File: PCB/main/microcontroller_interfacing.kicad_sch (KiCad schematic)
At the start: 11 parts, among them IC2 LM358DT, IC3 AT24C256C-SSHL-T, J9 PZ254V-11-02P

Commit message: new PCB
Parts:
- removed MCU1: STM32F030C8Tx, Package_QFP:LQFP-48_7x7mm_P0.5mm, symbol MCU_ST_STM32F0:STM32F030C8Tx
- J9: footprint HDRV2W64P0X254_1X2_508X250X873P -> SamacSys_Parts_Power:HDRV2W64P0X254_1X2_508X250X873P
- TP8, TP9: footprint SamacSys_Parts:5017 -> SamacSys_Parts_Power:5017
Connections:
- net NRST: now reaches C13.1, J9.1
- net SCL_P4 renamed PC15
- net SDA_P43 renamed PB7
- no-connect marks 36 -> 3
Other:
- moved on the sheet: IC3

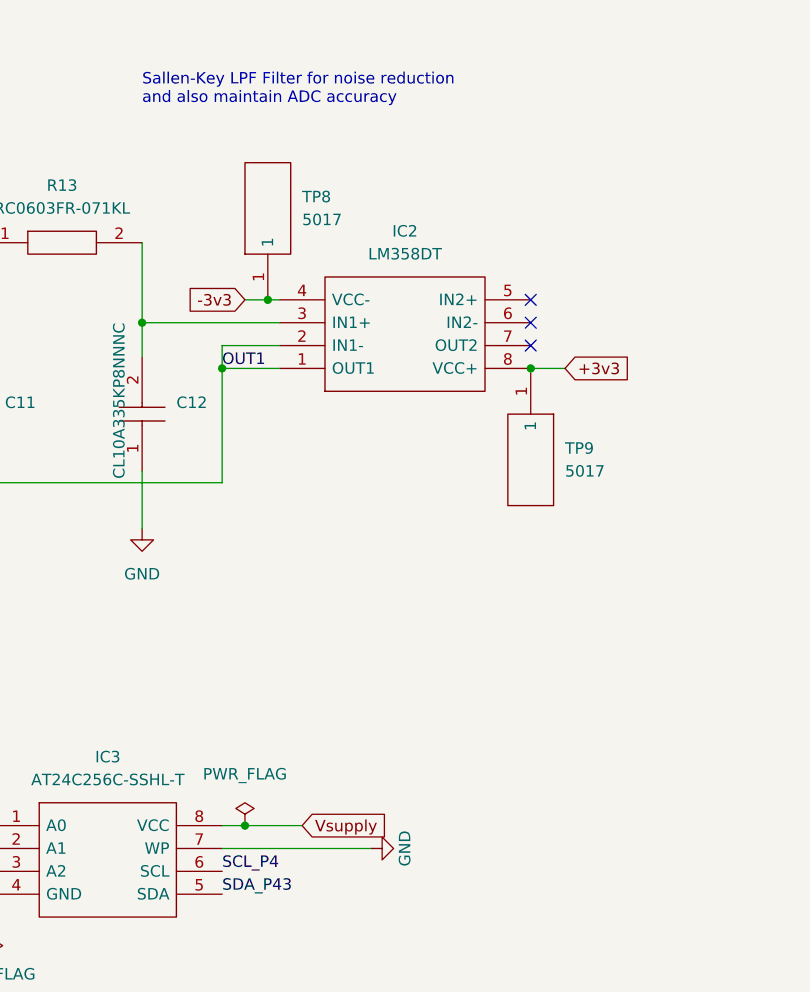
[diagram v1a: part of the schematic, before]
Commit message: changed power schematic
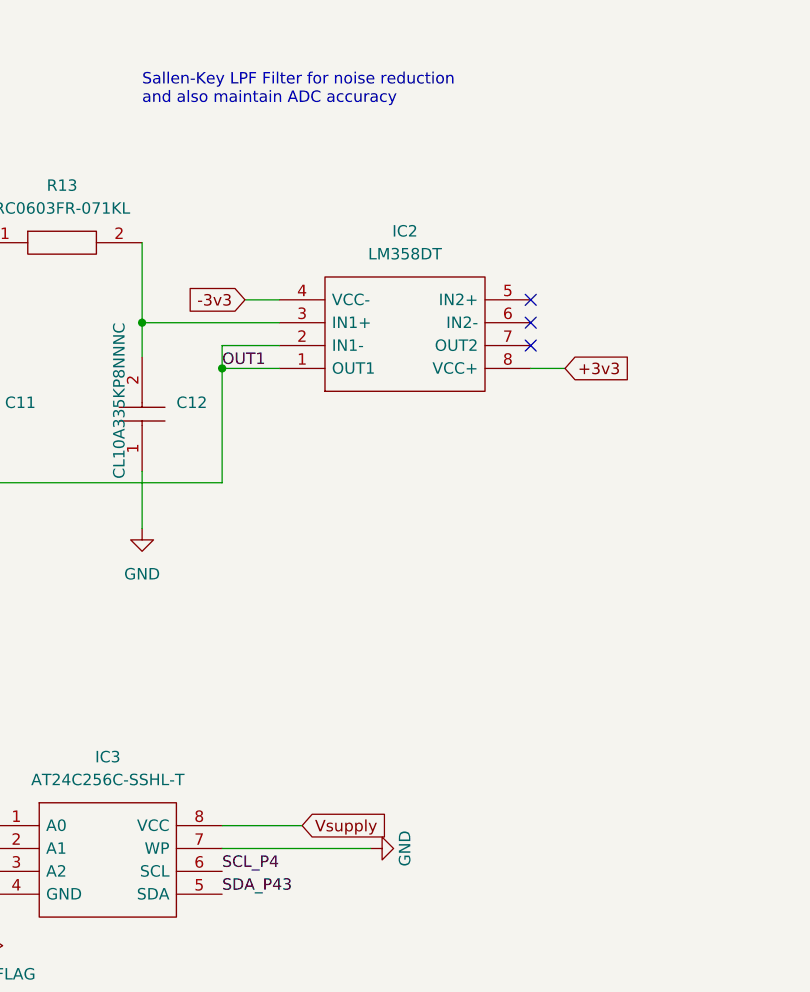
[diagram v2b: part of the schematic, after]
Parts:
- removed TP8, TP9: 5017, SamacSys_Parts_Power:5017, symbol SamacSys_Parts_power:5017
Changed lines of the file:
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@@
   (junction (at 78.74 68.58) (diameter 0) (color 0 0 0 0)
   )
-  (junction (at 121.92 73.66) (diameter 0) (color 0 0 0 0)
-  )
   (junction (at 55.88 127) (diameter 0) (color 0 0 0 0)
   )
-  (junction (at 90.17 124.46) (diameter 0) (color 0 0 0 0)
-  )
   (junction (at 87.63 73.66) (diameter 0) (color 0 0 0 0)
   )
@@
   )
   (junction (at 62.23 132.08) (diameter 0) (color 0 0 0 0)
-  )
-  (junction (at 92.71 66.04) (diameter 0) (color 0 0 0 0)
   )
   (junction (at 180.34 33.02) (diameter 0) (color 0 0 0 0)
@@
     (stroke (width 0) (type default) (color 0 0 0 0))
   )
-  (wire (pts (xy 87.63 124.46) (xy 90.17 124.46))
+  (wire (pts (xy 87.63 124.46) (xy 96.52 124.46))
     (stroke (width 0) (type default) (color 0 0 0 0))
   )
@@
     (stroke (width 0) (type default) (color 0 0 0 0))
   )
-  (wire (pts (xy 90.17 124.46) (xy 96.52 124.46))
-    (stroke (width 0) (type default) (color 0 0 0 0))
-  )
-  (wire (pts (xy 90.17 66.04) (xy 92.71 66.04))
+  (wire (pts (xy 90.17 66.04) (xy 93.98 66.04))
     (stroke (width 0) (type default) (color 0 0 0 0))
   )
@@
   )
   (wire (pts (xy 180.34 33.02) (xy 180.34 38.1))
-    (stroke (width 0) (type default) (color 0 0 0 0))
-  )
-  (wire (pts (xy 92.71 66.04) (xy 93.98 66.04))
     (stroke (width 0) (type default) (color 0 0 0 0))
   )
@@
     )
     (property "Datasheet" "" (id 3) (at 237.49 25.4 0)
-      (effects (font (size 1.27 1.27)) hide)
-    )
-    (pin "1")
-  )
-  (symbol (lib_id "power:PWR_FLAG") (at 90.17 124.46 0) (unit 1)
-    (in_bom yes) (on_board yes) (fields_autoplaced)
-    (property "Reference" "#FLG08" (id 0) (at 90.17 122.555 0)
-      (effects (font (size 1.27 1.27)) hide)
-    )
-    (property "Value" "PWR_FLAG" (id 1) (at 90.17 118.745 0))
-    (property "Footprint" "" (id 2) (at 90.17 124.46 0)
-      (effects (font (size 1.27 1.27)) hide)
-    )
-    (property "Datasheet" "~" (id 3) (at 90.17 124.46 0)
-      (effects (font (size 1.27 1.27)) hide)
-    )
-    (pin "1")
-  )
-  (symbol (lib_id "SamacSys_Parts_power:5017") (at 92.71 66.04 90) (unit 1)
-    (in_bom yes) (on_board yes) (fields_autoplaced)
-    (property "Reference" "TP8" (id 0) (at 96.52 54.6099 90)
-      (effects (font (size 1.27 1.27)) (justify right))
-    )
-    (property "Value" "5017" (id 1) (at 96.52 57.1499 90)
-      (effects (font (size 1.27 1.27)) (justify right))
-    )
-    (property "Footprint" "SamacSys_Parts_Power:5017" (id 2) (at 90.17 49.53 0)
-      (effects (font (size 1.27 1.27)) (justify left) hide)
-    )
-    (property "Datasheet" "http://www.keyelco.com/product.cfm/product_id/1355" (id 3) (at 92.71 49.53 0)
-      (effects (font (size 1.27 1.27)) (justify left) hide)
-    )
-    (property "Description" "KEYSTONE - 5017 - TEST POINT, PCB, MINIATURE, SMT" (id 4) (at 95.25 49.53 0)
-      (effects (font (size 1.27 1.27)) (justify left) hide)
-    )
-    (property "Height" "" (id 5) (at 97.79 49.53 0)
-      (effects (font (size 1.27 1.27)) (justify left) hide)
-    )
-    (property "Manufacturer_Name" "Keystone Electronics" (id 6) (at 100.33 49.53 0)
-      (effects (font (size 1.27 1.27)) (justify left) hide)
-    )
-    (property "Manufacturer_Part_Number" "5017" (id 7) (at 102.87 49.53 0)
-      (effects (font (size 1.27 1.27)) (justify left) hide)
-    )
-    (property "Mouser Part Number" "534-5017" (id 8) (at 105.41 49.53 0)
-      (effects (font (size 1.27 1.27)) (justify left) hide)
-    )
-    (property "Mouser Price/Stock" "https://www.mouser.co.uk/ProductDetail/Keystone-Electronics/5017?qs=Rc9fedAPY0Oq34lsnTvuLg%3D%3D" (id 9) (at 107.95 49.53 0)
-      (effects (font (size 1.27 1.27)) (justify left) hide)
-    )
-    (property "Arrow Part Number" "" (id 10) (at 110.49 49.53 0)
-      (effects (font (size 1.27 1.27)) (justify left) hide)
-    )
-    (property "Arrow Price/Stock" "" (id 11) (at 113.03 49.53 0)
-      (effects (font (size 1.27 1.27)) (justify left) hide)
-    )
-    (property "Comment" "test point" (id 12) (at 92.71 66.04 0)
-      (effects (font (size 1.27 1.27)) hide)
-    )
-    (property "JLCPCB Part Number" "C238130" (id 13) (at 92.71 66.04 0)
-      (effects (font (size 1.27 1.27)) hide)
-    )
-    (property "LCSC" "C238130" (id 14) (at 92.71 66.04 0)
-      (effects (font (size 1.27 1.27)) hide)
-    )
-    (property "Price($)" "0.4796" (id 15) (at 92.71 66.04 0)
       (effects (font (size 1.27 1.27)) hide)
     )
@@
       (effects (font (size 1.27 1.27)) hide)
     )
-    (pin "1")
-  )
-  (symbol (lib_id "SamacSys_Parts_power:5017") (at 121.92 73.66 270) (unit 1)
-    (in_bom yes) (on_board yes) (fields_autoplaced)
-    (property "Reference" "TP9" (id 0) (at 125.73 82.5499 90)
-      (effects (font (size 1.27 1.27)) (justify left))
-    )
-    (property "Value" "5017" (id 1) (at 125.73 85.0899 90)
-      (effects (font (size 1.27 1.27)) (justify left))
-    )
-    (property "Footprint" "SamacSys_Parts_Power:5017" (id 2) (at 124.46 90.17 0)
-      (effects (font (size 1.27 1.27)) (justify left) hide)
-    )
-    (property "Datasheet" "http://www.keyelco.com/product.cfm/product_id/1355" (id 3) (at 121.92 90.17 0)
-      (effects (font (size 1.27 1.27)) (justify left) hide)
-    )
-    (property "Description" "KEYSTONE - 5017 - TEST POINT, PCB, MINIATURE, SMT" (id 4) (at 119.38 90.17 0)
-      (effects (font (size 1.27 1.27)) (justify left) hide)
-    )
-    (property "Height" "" (id 5) (at 116.84 90.17 0)
-      (effects (font (size 1.27 1.27)) (justify left) hide)
-    )
-    (property "Manufacturer_Name" "Keystone Electronics" (id 6) (at 114.3 90.17 0)
-      (effects (font (size 1.27 1.27)) (justify left) hide)
-    )
-    (property "Manufacturer_Part_Number" "5017" (id 7) (at 111.76 90.17 0)
-      (effects (font (size 1.27 1.27)) (justify left) hide)
-    )
-    (property "Mouser Part Number" "534-5017" (id 8) (at 109.22 90.17 0)
-      (effects (font (size 1.27 1.27)) (justify left) hide)
-    )
-    (property "Mouser Price/Stock" "https://www.mouser.co.uk/ProductDetail/Keystone-Electronics/5017?qs=Rc9fedAPY0Oq34lsnTvuLg%3D%3D" (id 9) (at 106.68 90.17 0)
-      (effects (font (size 1.27 1.27)) (justify left) hide)
-    )
-    (property "Arrow Part Number" "" (id 10) (at 104.14 90.17 0)
-      (effects (font (size 1.27 1.27)) (justify left) hide)
-    )
-    (property "Arrow Price/Stock" "" (id 11) (at 101.6 90.17 0)
-      (effects (font (size 1.27 1.27)) (justify left) hide)
-    )
-    (property "Comment" "test point" (id 12) (at 121.92 73.66 0)
-      (effects (font (size 1.27 1.27)) hide)
-    )
-    (property "JLCPCB Part Number" "C238130" (id 13) (at 121.92 73.66 0)
-      (effects (font (size 1.27 1.27)) hide)
-    )
-    (property "LCSC" "C238130" (id 14) (at 121.92 73.66 0)
-      (effects (font (size 1.27 1.27)) hide)
-    )
-    (property "Price($)" "0.4796" (id 15) (at 121.92 73.66 0)
-      (effects (font (size 1.27 1.27)) hide)
-    )

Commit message: NEW PCB ADDED
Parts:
- C13: footprint CAPC1608X90N -> SamacSys_Parts:CAPC1608X90N
- J9: footprint SamacSys_Parts_Power:HDRV2W64P0X254_1X2_508X250X873P -> SamacSys_Parts:HDRV2W64P0X254_1X2_508X250X873P; Comment 2 pin male header -> pin header (2x1)
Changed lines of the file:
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@@
       (effects (font (size 1.27 1.27)) (justify left))
     )
-    (property "Footprint" "SamacSys_Parts_Power:HDRV2W64P0X254_1X2_508X250X873P" (id 2) (at 252.73 40.64 0)
+    (property "Footprint" "SamacSys_Parts:HDRV2W64P0X254_1X2_508X250X873P" (id 2) (at 252.73 40.64 0)
       (effects (font (size 1.27 1.27)) (justify left) hide)
     )
@@
       (effects (font (size 1.27 1.27)) (justify left) hide)
     )
-    (property "Comment" "2 pin male header" (id 12) (at 236.22 43.18 0)
+    (property "Comment" "pin header (2x1)" (id 12) (at 236.22 43.18 0)
       (effects (font (size 1.27 1.27)) hide)
     )
@@
       (effects (font (size 1.27 1.27)) (justify right))
     )
-    (property "Footprint" "CAPC1608X90N" (id 2) (at 222.25 30.48 0)
+    (property "Footprint" "SamacSys_Parts:CAPC1608X90N" (id 2) (at 222.25 30.48 0)
       (effects (font (size 1.27 1.27)) (justify left) hide)
     )
